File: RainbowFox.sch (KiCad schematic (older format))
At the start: 157 parts

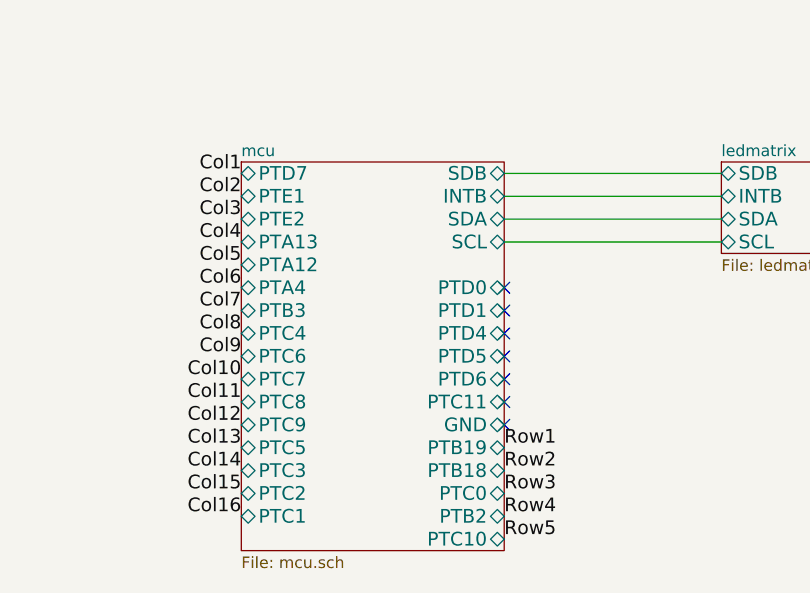
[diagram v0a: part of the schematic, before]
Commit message: Switched to different Debug Ports
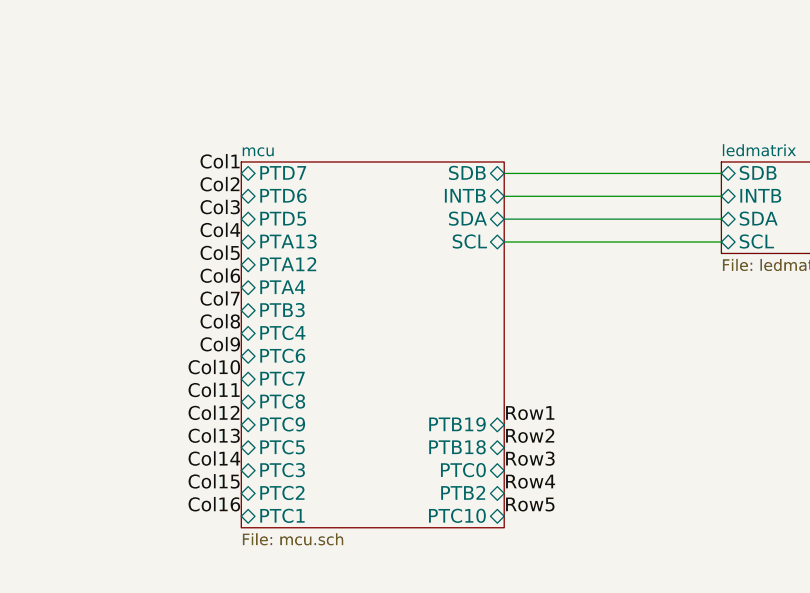
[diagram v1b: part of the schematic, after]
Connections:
- no-connect marks 7 -> 0
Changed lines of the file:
@@
 Text Label 8400 7050 2    60   ~ 0
 Col9
+Text Label 9550 7350 0    60   ~ 0
+Row1
 Text Label 9550 7450 0    60   ~ 0
-Row1
+Row2
 Text Label 9550 7550 0    60   ~ 0
-Row2
+Row3
 Text Label 9550 7650 0    60   ~ 0
-Row3
+Row4
 Text Label 9550 7750 0    60   ~ 0
-Row4
-Text Label 9550 7850 0    60   ~ 0
 Row5
 $Comp
@@
 	10500 6550 9550 6550
 $Sheet
-S 8400 6200 1150 1700
+S 8400 6200 1150 1600
 U 549878F0
 F0 "mcu" 50
 F1 "mcu.sch" 50
 F2 "PTA4" T L 8400 6750 60
-F3 "PTB2" T R 9550 7750 60
+F3 "PTB2" T R 9550 7650 60
 F4 "PTB3" T L 8400 6850 60
-F5 "PTC0" T R 9550 7650 60
-F6 "GND" B R 9550 7350 60
-F7 "PTA12" T L 8400 6650 60
-F8 "PTA13" T L 8400 6550 60
-F9 "PTB19" T R 9550 7450 60
-F10 "PTB18" T R 9550 7550 60
-F11 "PTC11" T R 9550 7250 60
-F12 "PTC9" T L 8400 7350 60
-F13 "PTC10" T R 9550 7850 60
-F14 "PTD0" T R 9550 6750 60
-F15 "PTD1" T R 9550 6850 60
-F16 "PTD4" T R 9550 6950 60
-F17 "PTD5" T R 9550 7050 60
-F18 "PTD6" T R 9550 7150 60
-F19 "PTD7" T L 8400 6250 60
-F20 "PTC1" T L 8400 7750 60
-F21 "PTC2" T L 8400 7650 60
-F22 "PTC3" T L 8400 7550 60
-F23 "PTC7" T L 8400 7150 60
-F24 "PTC6" T L 8400 7050 60
-F25 "PTC5" T L 8400 7450 60
-F26 "PTC4" T L 8400 6950 60
-F27 "PTC8" T L 8400 7250 60
-F28 "PTE1" B L 8400 6350 60
-F29 "PTE2" B L 8400 6450 60
-F30 "SDB" B R 9550 6250 60
-F31 "INTB" B R 9550 6350 60
-F32 "SDA" B R 9550 6450 60
-F33 "SCL" B R 9550 6550 60
+F5 "PTC0" T R 9550 7550 60
+F6 "PTA12" T L 8400 6650 60
+F7 "PTA13" T L 8400 6550 60
+F8 "PTB19" T R 9550 7350 60
+F9 "PTB18" T R 9550 7450 60
+F10 "PTC9" T L 8400 7350 60
+F11 "PTC10" T R 9550 7750 60
+F12 "PTD5" T L 8400 6450 60
+F13 "PTD6" T L 8400 6350 60
+F14 "PTD7" T L 8400 6250 60
+F15 "PTC1" T L 8400 7750 60
+F16 "PTC2" T L 8400 7650 60
+F17 "PTC3" T L 8400 7550 60
+F18 "PTC7" T L 8400 7150 60
+F19 "PTC6" T L 8400 7050 60
+F20 "PTC5" T L 8400 7450 60
+F21 "PTC4" T L 8400 6950 60
+F22 "PTC8" T L 8400 7250 60
+F23 "SDB" B R 9550 6250 60
+F24 "INTB" B R 9550 6350 60
+F25 "SDA" B R 9550 6450 60
+F26 "SCL" B R 9550 6550 60
 $EndSheet
-NoConn ~ 9550 7350
-NoConn ~ 9550 7250
-NoConn ~ 9550 7150
-NoConn ~ 9550 7050
-NoConn ~ 9550 6950
-NoConn ~ 9550 6850
-NoConn ~ 9550 6750
 $EndSCHEMATC
